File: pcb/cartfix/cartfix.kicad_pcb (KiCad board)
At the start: 2 copper layers, 18 x 44 mm, 2 parts, among them J1 CONN_02X16, J2 CONN_02X16

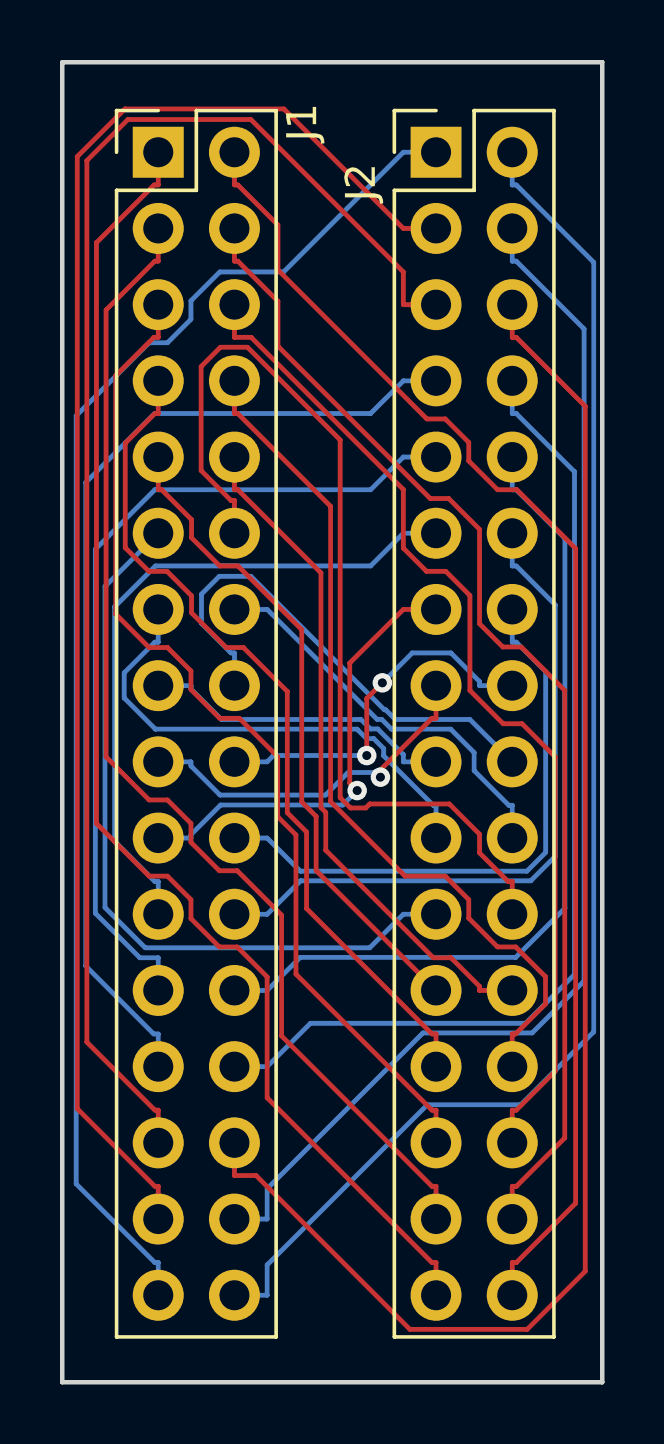
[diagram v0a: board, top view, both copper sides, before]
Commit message: Migrate other PCBs from KiCad 4 to KiCad 8
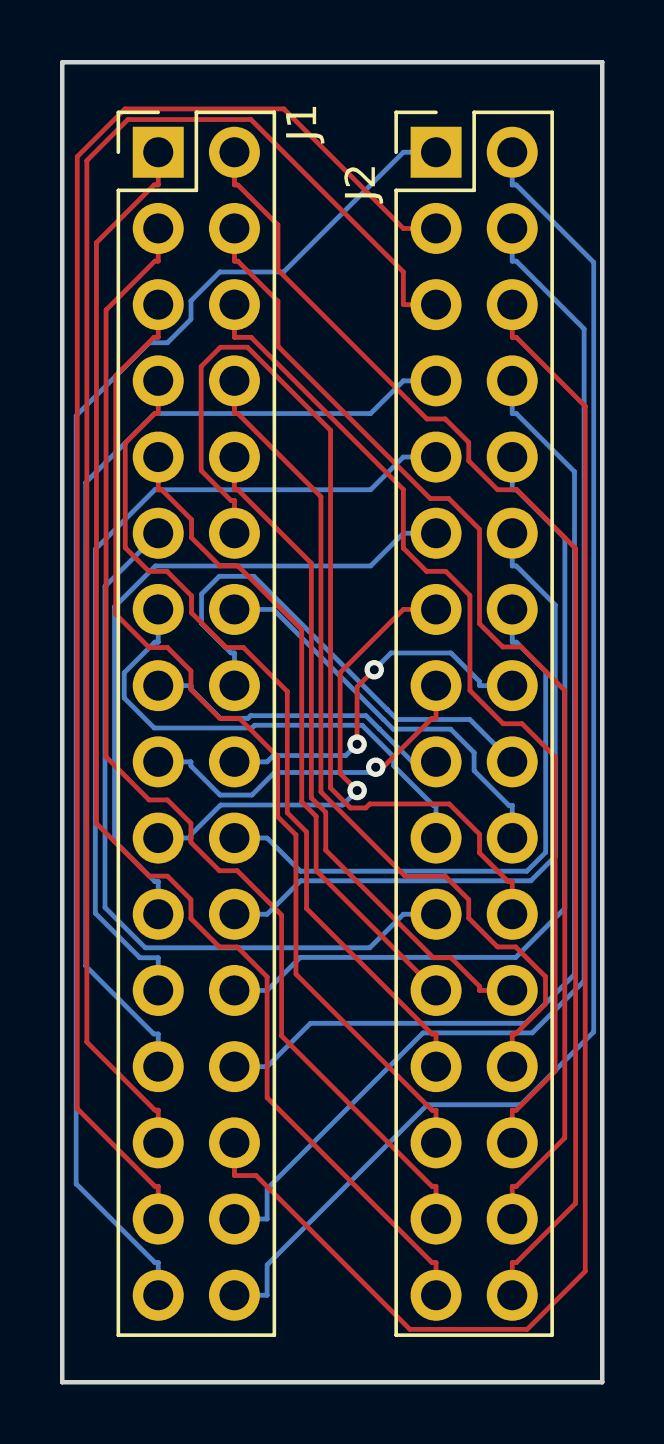
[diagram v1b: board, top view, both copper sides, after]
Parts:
- J1, J2: value CONN_02X16 -> Conn_02x16_Odd_Even; footprint Pin_Headers:Pin_Header_Straight_2x16_Pitch2.54mm -> Connector_PinHeader_2.54mm:PinHeader_2x16_P2.54mm_Vertical
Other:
- net class Default removed
